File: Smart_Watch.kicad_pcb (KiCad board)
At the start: 2 copper layers, 59 parts, among them J1 USB_C_Receptacle, J2 Conn_01x02, J3 Conn_01x06, J4 Conn_01x02, SW2 SW_Push, SW3 SW_Push, SW4 SW_Push, SW5 SW_Push, SW6 SW_Push, SW7 SW_Push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

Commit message: Layout V1
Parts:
- C1, C2, C21, C23, C26, C3, C4, C5, C6, C8, C9, J2, J3, NT3, R1, R2, R3, SW2, SW3, U1, U10, U2, U4, U5: moved to B.Cu
- moved R2 168.6 mm to (175.2, 99.0), turned to 180 degrees
- moved R1 168.6 mm to (175.2, 100.5), turned to 180 degrees
- moved NT3 166.9 mm to (174.3, 102.3)
- moved C8 164.5 mm to (175.9, 107.6), turned to -90 degrees
- moved C9 162.6 mm to (173.3, 105.0)
- moved U4 162.5 mm to (176.3, 104.8)
- moved U1 161.6 mm to (171.3, 101.2), turned to 180 degrees
- moved SW4 156.8 mm to (182.2, 97.8), turned to 135 degrees
- moved C3 155.9 mm to (168.3, 103.7)
- moved C2 155.8 mm to (168.3, 100.4)
- moved R3 154.4 mm to (167.5, 98.1), turned to 180 degrees
- moved C4 152.7 mm to (166.6, 103.7)
- moved C1 152.6 mm to (166.6, 100.4)
- moved SW6 151.4 mm to (182.1, 117.8), turned to 45 degrees
- moved J1 149.3 mm to (172.2, 119.3)
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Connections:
- net Net-(J2-Pin_1) renamed /Architecture/Peripherals/MOTOR+
- net Net-(J2-Pin_2) renamed /Architecture/Peripherals/MOTOR-
- net Net-(U6-VSET1) renamed /Architecture/Power/VSET1
- net Net-(U6-VSET2) renamed /Architecture/Power/VSET2
- net Net-(U8-ISET) renamed /Architecture/MCU/ISET
- net Net-(U9-P0.00/XL1) renamed /Architecture/MCU/CLK1
- net Net-(U9-P0.01/XL2) renamed /Architecture/MCU/CLK2
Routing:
- net GND: track 0.00 -> 130.2 mm
- net VSYS: track 0.00 -> 41.9 mm
- net +1V8: track 0.00 -> 39.5 mm
- net /Architecture/MCU/CLK1: track 0.00 -> 14.7 mm, vias 0 -> 2
- net /Architecture/MCU/DISPLAY_LIGHT_IO: track 0.00 -> 9.56 mm, vias 0 -> 2
- net /Architecture/MCU/MCU_RST: track 0.00 -> 8.30 mm
- net +BATT: track 0.00 -> 7.81 mm
- net /Architecture/MCU/VBUS_IN: track 0.00 -> 6.81 mm
- net /Architecture/MCU/SCL: track 0.00 -> 6.47 mm
- net /Architecture/Power/SW2: track 0.00 -> 4.82 mm
- net +3V0: track 0.00 -> 4.69 mm
- net /Architecture/MCU/VBUS_OUT: track 0.00 -> 4.33 mm
- net /Architecture/MCU/CLK2: track 0.00 -> 3.30 mm
- net /Architecture/Power/VSET1: track 0.00 -> 2.88 mm
- net /Architecture/MCU/MAX_INT: track 0.00 -> 2.35 mm
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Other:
- board outline added: 32 x 32 mm
- copper layers 2 -> 4

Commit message: I hate you git
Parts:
- moved C23 18.3 mm to (159.1, 113.8)
- moved J2 17.1 mm to (165.8, 115.0)
- moved U10 17.0 mm to (163.1, 114.9)
- moved C9 12.3 mm to (180.1, 115.3), turned to 0 degrees
- moved J3 9.78 mm to (179.1, 118.9), turned to -90 degrees
- moved U4 9.12 mm to (179.6, 113.3)
- moved C8 5.49 mm to (177.6, 112.8), turned to 90 degrees
- moved C26 3.57 mm to (160.1, 107.2)
- moved C21 3.57 mm to (160.2, 108.7)
- moved U5 3.28 mm to (167.1, 109.1)
- moved C5 2.08 mm to (176.3, 98.6)
- moved C6 2.08 mm to (172.2, 96.2)
- moved U2 2.08 mm to (175.8, 95.4)
- moved L2 2.07 mm to (161.2, 103.3)
- moved NT3 2.06 mm to (172.3, 101.7)
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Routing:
- net GND: track 130.2 -> 0.00 mm
- net VSYS: track 41.9 -> 9.82 mm
- net +1V8: track 39.5 -> 9.24 mm
- net /Architecture/MCU/CLK1: track 14.7 -> 0.00 mm, vias 2 -> 0
- net /Architecture/MCU/DISPLAY_LIGHT_IO: track 9.56 -> 0.00 mm, vias 2 -> 0
- net /Architecture/MCU/MCU_RST: track 8.30 -> 0.00 mm
- net /Architecture/MCU/SCL: track 6.47 -> 0.00 mm
- net +BATT: track 7.81 -> 1.96 mm
- net /Architecture/MCU/VBUS_IN: track 6.81 -> 2.94 mm
- net +3V0: track 4.69 -> 1.33 mm
- net /Architecture/MCU/CLK2: track 3.30 -> 0.00 mm
- net /Architecture/MCU/MAX_INT: track 2.35 -> 0.00 mm
- net /Architecture/Peripherals/MOTOR-: track 1.95 -> 0.00 mm
- net /Architecture/Peripherals/MOTOR+: track 1.91 -> 0.00 mm
- net /Architecture/MCU/USBC_D-: track 1.63 -> 0.00 mm
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- added copper zone on B.Cu, net GND
- added copper zone on F.Cu, net GND
- added copper zone on In1.Cu, net GND
- added copper zone on In2.Cu, net GND

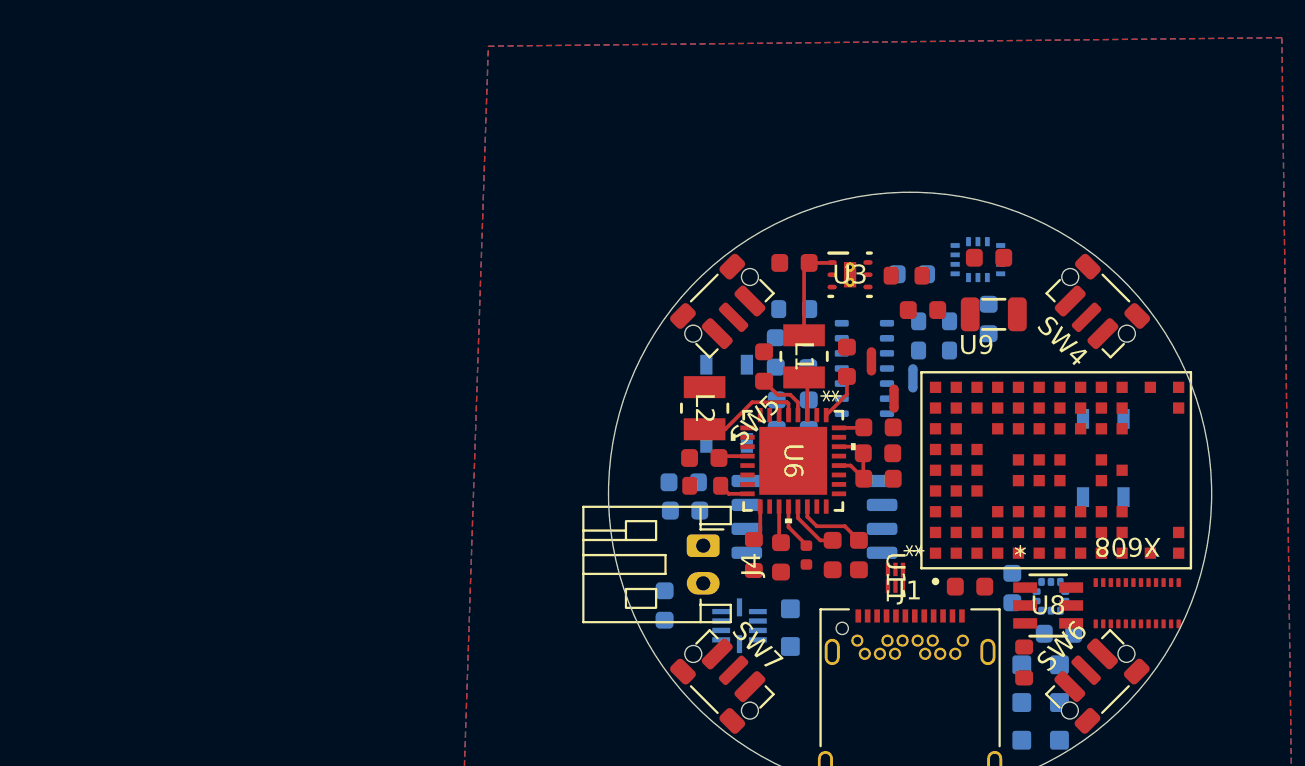
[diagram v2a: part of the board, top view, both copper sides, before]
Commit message: Update most sym/footprint libraries
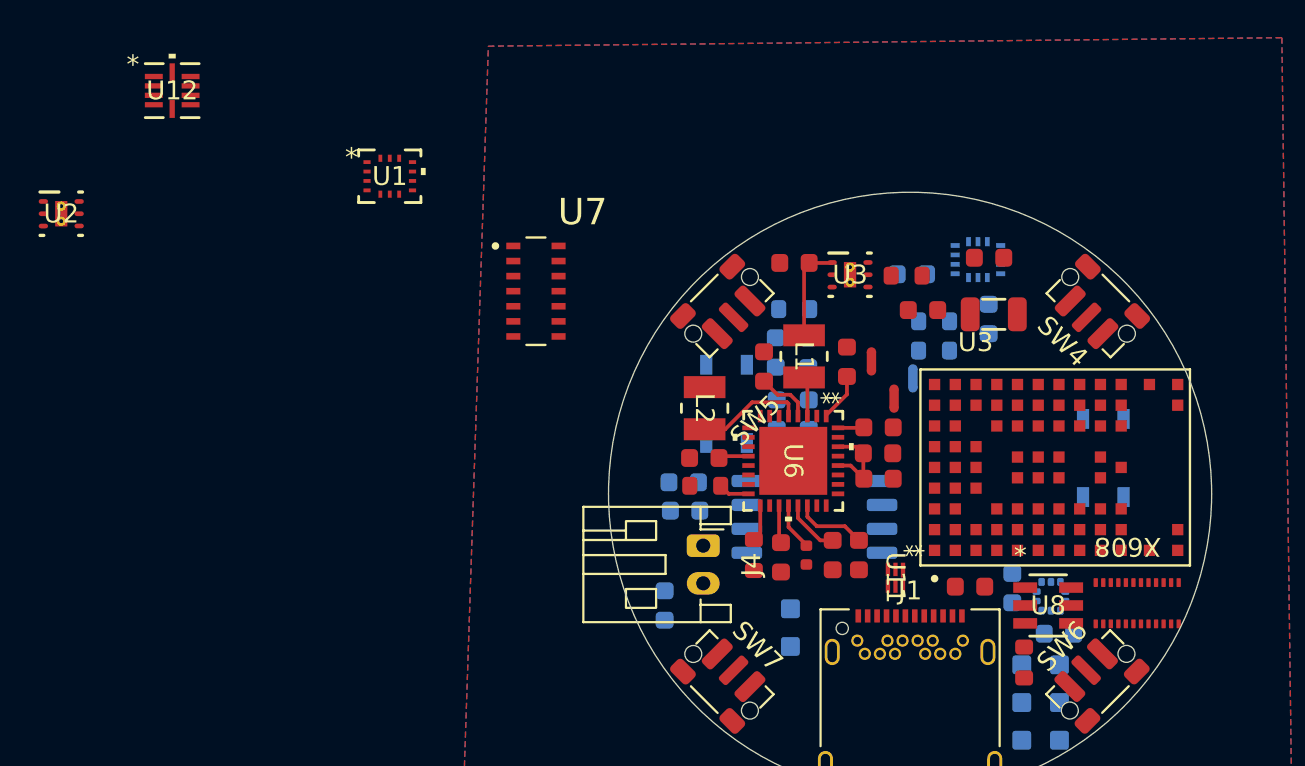
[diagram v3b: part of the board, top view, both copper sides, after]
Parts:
- removed U10: DRV2603RUNR, DRV:RUN10_TEX
- removed U9: NORA-B106-00B, NORA-B106-00B:XCVR_NORA-B106-00B
- added U12: DRV2603RUNR, Smart_Watch:RUN10_TEX, F.Cu at (133.0, 86.5)
- added U2: OPT3004DNPR, Smart_Watch:DNP0006A, F.Cu at (127.1, 93.0)
- added U3: NORA-B106-00B, Smart_Watch:XCVR_NORA-B106-00B, F.Cu at (179.8, 106.5)
- added U7: MAX30102EFD_T, Smart_Watch:XDCR_MAX30101EFD_, F.Cu at (152.3, 97.1)
- U1: value MAX30102 -> BMI270; footprint OptoDevice:Maxim_OLGA-14_3.3x5.6mm_P0.8mm -> Smart_Watch:BMI270_BOS-L; moved to F.Cu
- U6: footprint NPM:QFN32_5X5_NOR -> Smart_Watch:QFN32_5X5_NOR-L
- moved U1 27.2 mm to (144.5, 91.0), turned to 0 degrees
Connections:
- C1 pad 1: +1V8 -> GND
- C1 pad 2: GND -> +1V8
- C2 pad 1: +1V8 -> GND
- C2 pad 2: GND -> +1V8
- NT3 pad 1: PGND3 -> GND
- NT3 pad 2: GND -> PGND3
- R1 pad 1: +1V8 -> VDD
- R1 pad 2: /Architecture/MCU/SDA -> unconnected-(R1-Pad2)
- R2 pad 1: +1V8 -> VDD
- R2 pad 2: /Architecture/MCU/SCL -> unconnected-(R2-Pad2)
- U1 pad 1: unconnected-(U1-NC-Pad1) -> GND
- U1 pad 10: +1V8 -> unconnected-(U1-OCSB-Pad10)
- U1 pad 11: +1V8 -> unconnected-(U1-OSDO-Pad11)
- U1 pad 12: GND -> +1V8
- U1 pad 13: /Architecture/MCU/MAX_INT -> /Architecture/MCU/SCL
- U1 pad 14: unconnected-(U1-NC-Pad14) -> /Architecture/MCU/SDA
- U1 pad 2: /Architecture/MCU/SCL -> unconnected-(U1-ASDX-Pad2)
- U1 pad 3: /Architecture/MCU/SDA -> unconnected-(U1-ASCX-Pad3)
- U1 pad 4: PGND3 -> unconnected-(U1-INT1-Pad4)
- U1 pad 5: unconnected-(U1-NC-Pad5) -> +1V8
- U1 pad 6: unconnected-(U1-NC-Pad6) -> GND
- U1 pad 7: unconnected-(U1-NC-Pad7) -> GND
- U1 pad 8: unconnected-(U1-NC-Pad8) -> +1V8
- U1 pad 9: +1V8 -> /Architecture/MCU/BMI_INT

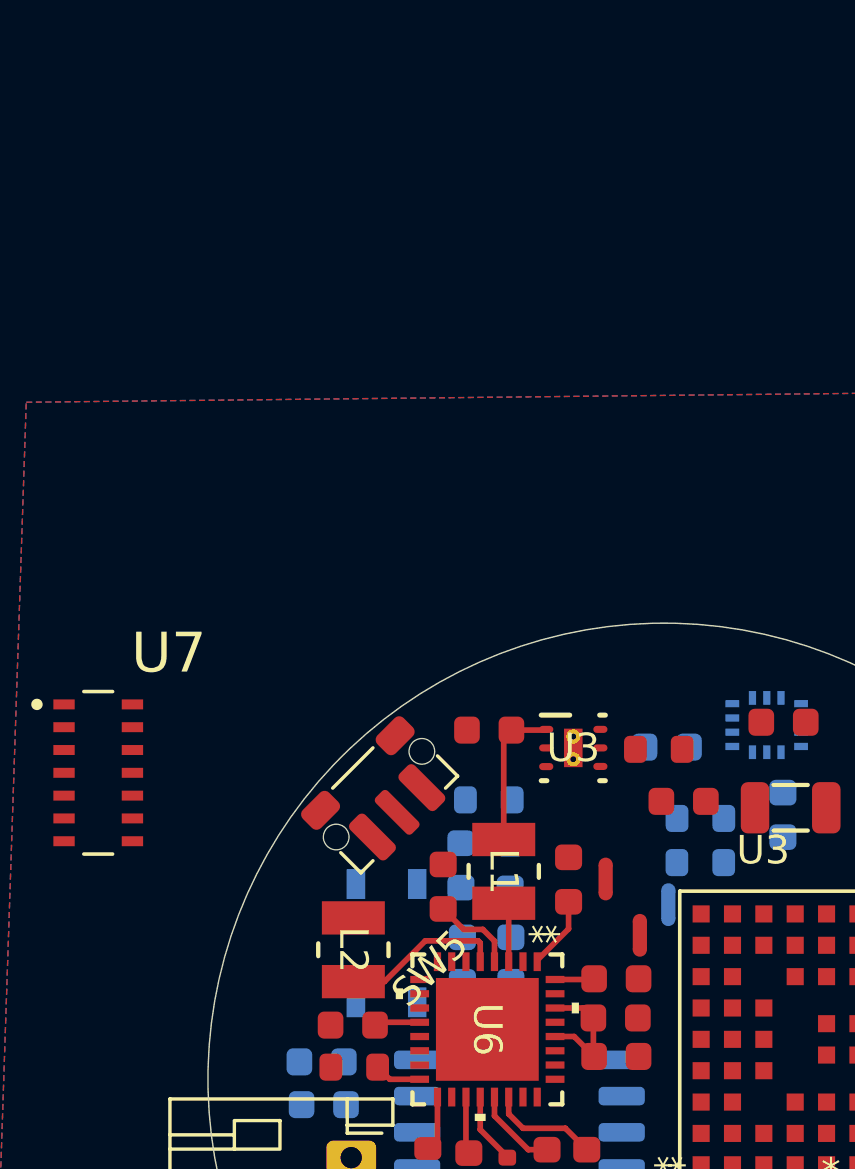
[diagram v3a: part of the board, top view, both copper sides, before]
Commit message: Switch inductors
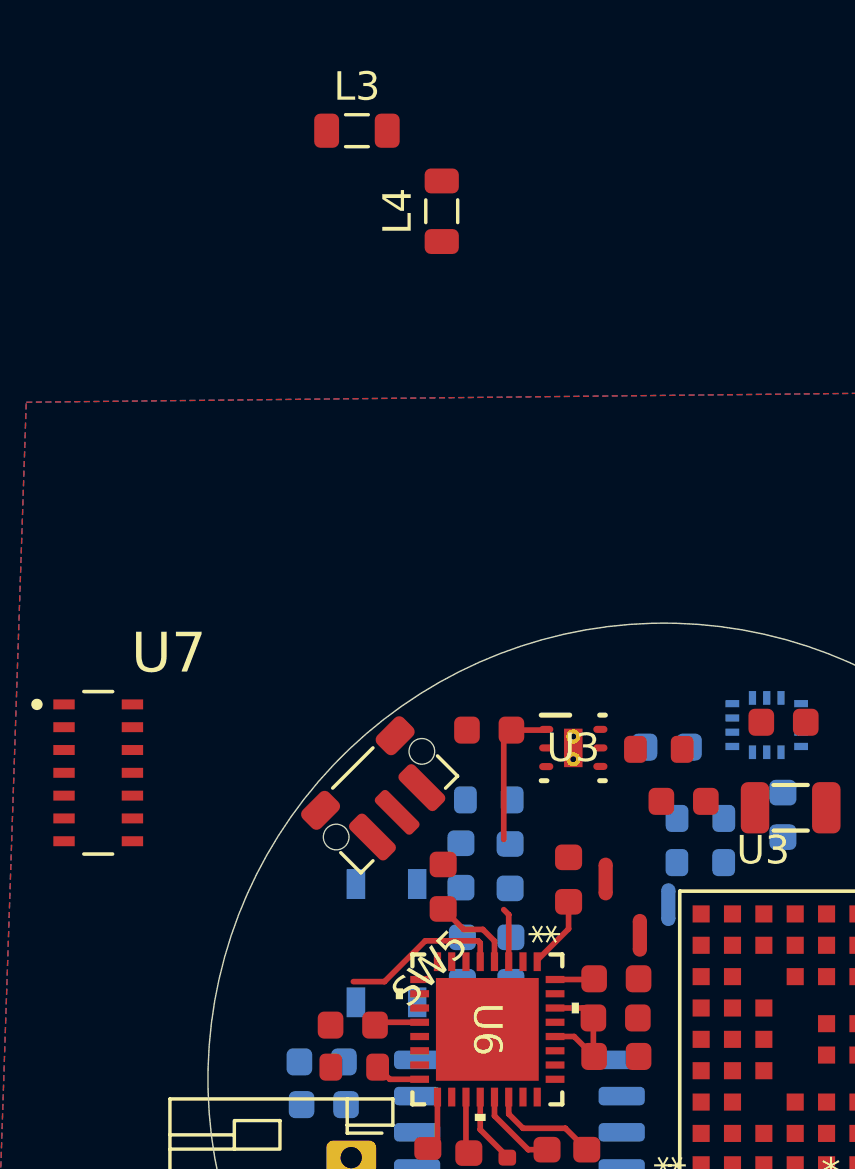
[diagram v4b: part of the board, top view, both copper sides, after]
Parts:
- removed L1, L2: LQM2HPN2R2MG0L, LQM:IND_LQM2HPN2R2MG0L_MUR
- added L3: 2.2uH, Inductor_SMD:L_0805_2012Metric, F.Cu at (161.4, 74.6)
- added L4: 2.2uH, Inductor_SMD:L_0805_2012Metric, F.Cu at (164.3, 77.4)
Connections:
- R1 pad 2: unconnected-(R1-Pad2) -> /Architecture/MCU/SDA
- R2 pad 2: unconnected-(R2-Pad2) -> /Architecture/MCU/SCL

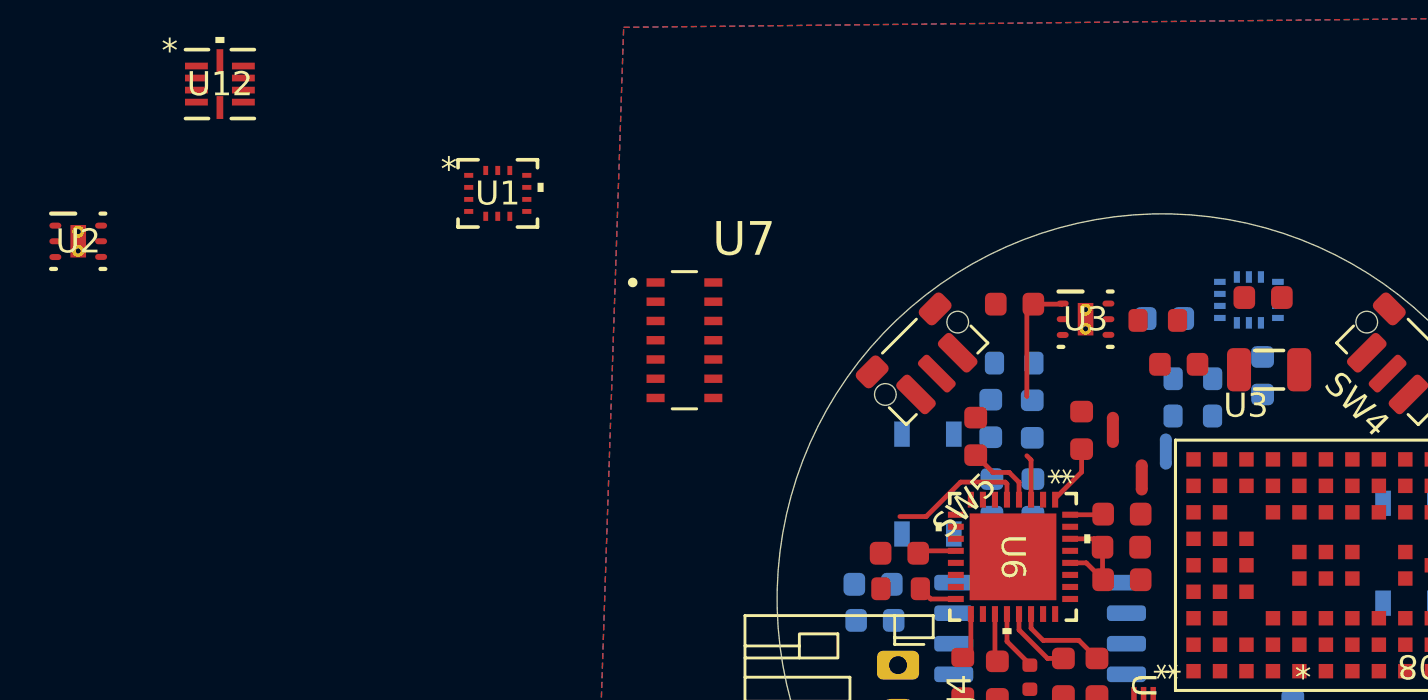
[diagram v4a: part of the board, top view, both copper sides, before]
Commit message: Change more footprints
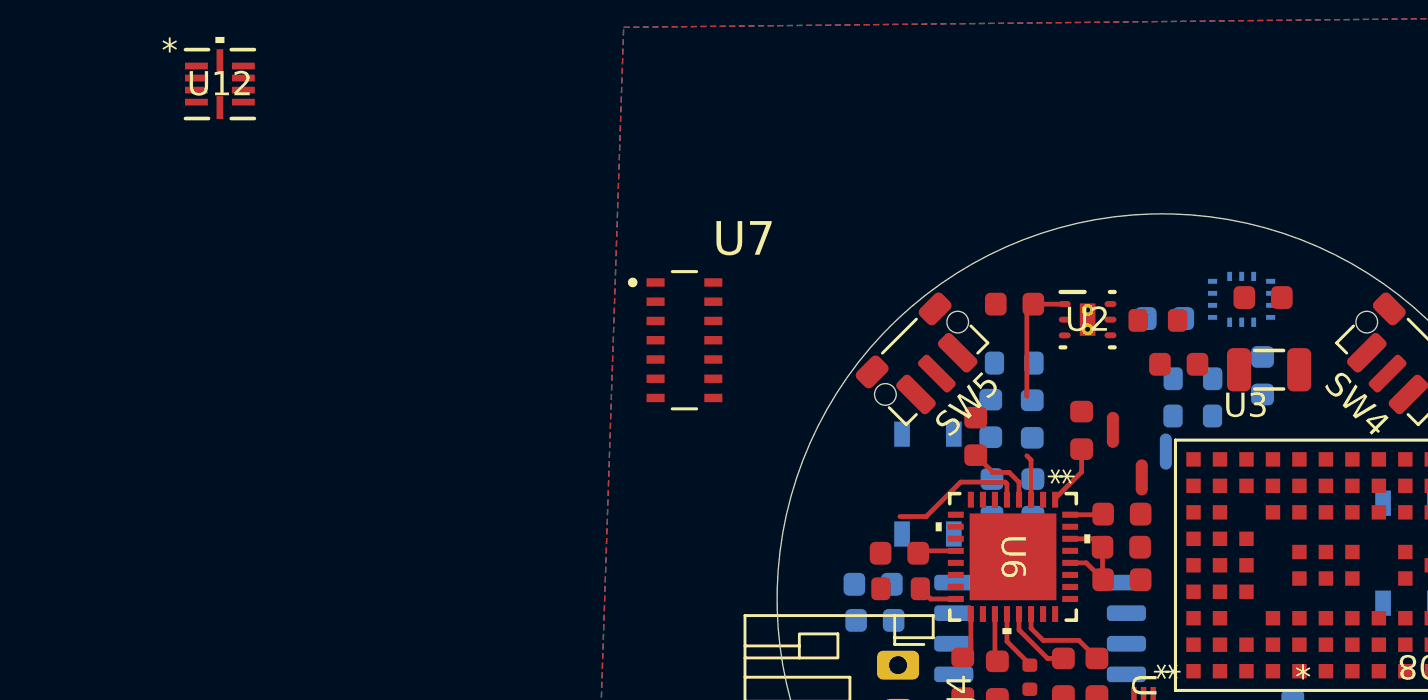
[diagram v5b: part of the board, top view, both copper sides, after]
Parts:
- removed the U2 at (175.8, 95.4)
- removed the U3 at (169.0, 96.2)
- SW4, SW5, SW6, SW7: footprint Button_Switch_SMD:SW_Push_1P1T-MP_NO_Horizontal_Alps_SKRTLAE010 -> Smart_Watch:SW_Push_1P1T-MP_NO_Horizontal_Alps_SKRTLAE010_3D
- U1: moved to B.Cu
- moved U2 42.1 mm to (169.1, 96.2)
- moved U1 31.2 mm to (175.4, 95.4), turned to 180 degrees

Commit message: WIP changes
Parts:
- removed J1: USB_C_Receptacle, Connector_USB:USB_C_Receptacle_Amphenol_12401548E4-2A
- added J5: USB_C_Receptacle_USB2.0_16P, Connector_USB:USB_C_Receptacle_GCT_USB4105-xx-A_16P_TopMnt_Horizontal, B.Cu at (172.2, 94.7)
- C1, C2, C21, C23, C26, C3, C4, C5, C6, C8, C9, J2, J3, NT3, R1, R2, R3, U1, U4, U5: moved to F.Cu
- SW2, SW3: footprint SKRPACE:SW_SKRPACE010_AAL -> Resistor_SMD:R_0805_2012Metric; moved to F.Cu
- SW4, SW5, SW6, SW7: moved to B.Cu
- moved C23 77.4 mm to (232.0, 139.8)
- moved C26 75.5 mm to (231.0, 133.3), turned to 0 degrees
- moved C21 75.3 mm to (230.9, 134.8), turned to 0 degrees
- moved C1 66.4 mm to (226.1, 126.4)
- moved C4 66.3 mm to (226.1, 129.7)
- moved J2 65.0 mm to (225.3, 141.0)
- moved R3 64.6 mm to (225.1, 124.1), turned to 0 degrees
- moved C2 63.2 mm to (224.4, 126.4)
- moved C3 63.2 mm to (224.3, 129.7)
- moved SW2 60.9 mm to (222.9, 110.0)
- moved C6 53.4 mm to (218.9, 122.2), turned to 0 degrees
- moved NT3 53.3 mm to (218.8, 127.8)
- moved U1 51.6 mm to (223.2, 115.0), turned to 0 degrees
- moved R1 51.4 mm to (217.7, 126.3), turned to 0 degrees
- moved R2 51.4 mm to (217.7, 124.8), turned to 0 degrees
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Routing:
- net VSYS: track 9.82 -> 0.00 mm
- net +1V8: track 9.24 -> 0.00 mm
- net /Architecture/Power/SW2: track 5.68 -> 0.00 mm
- net /Architecture/MCU/VBUS_OUT: track 3.80 -> 0.00 mm
- net /Architecture/MCU/VBUS_IN: track 2.94 -> 0.00 mm
- net +BATT: track 1.96 -> 0.00 mm
- net /Architecture/Power/VSET1: track 1.89 -> 0.00 mm
- net /Architecture/Power/SW1: track 1.85 -> 0.00 mm
- net /Architecture/Power/VSET2: track 1.60 -> 0.00 mm
- net +3V0: track 1.33 -> 0.00 mm
